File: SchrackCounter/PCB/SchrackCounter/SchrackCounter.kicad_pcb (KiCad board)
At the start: 4 copper layers, 98 x 88 mm, 61 parts, among them J1 Conn_01x02_Pin, J2 TYPE-C-31-M-12 (USB C CONN), J3 MEM2067-02-180-00-A_REVB, SW1 SW_Push, SW2 SW_Push, SW3 SW_Push, SW4 SW_Push, SW5 SW_Push, U1 LM1084-3.3, U2 LDD080AUE-101A, U3 LTD080AUE-103A, U4 LDD080AUE-101A, U5 MAX7219, U6 ESP32-S3-WROOM-2, U7 USBLC6-2SC6

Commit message: PCB update
pcb redesign
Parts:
- removed the J1 at (164.3, 128.1)
- added D2: LED, LED_SMD:LED_0805_2012Metric_Pad1.15x1.40mm_HandSolder, F.Cu at (179.8, 119.3)
- added D3: LED, LED_SMD:LED_0805_2012Metric_Pad1.15x1.40mm_HandSolder, F.Cu at (173.8, 119.3)
- added R6: 220R, Resistor_SMD:R_0805_2012Metric_Pad1.20x1.40mm_HandSolder, B.Cu at (181.7, 119.4)
- added R7: 220R, Resistor_SMD:R_0805_2012Metric_Pad1.20x1.40mm_HandSolder, B.Cu at (175.8, 119.3)
- added SW1: SW_SPST, Connector_JST:JST_XH_B2B-XH-A_1x02_P2.50mm_Vertical, F.Cu at (161.8, 126.8)
- R5: moved to B.Cu
- U5: footprint Package_DIP:DIP-24_W10.16mm -> Package_SO:SOP-24_7.5x15.4mm_P1.27mm; moved to B.Cu
- U6: moved to F.Cu
- moved BZ1 98.5 mm to (176.8, 130.6), turned to -90 degrees
- moved R5 89.4 mm to (184.2, 132.8), turned to 90 degrees
- moved U6 65.5 mm to (228.5, 103.6), turned to -90 degrees
- moved TP1 48.1 mm to (240.0, 65.6)
- moved C8 37.6 mm to (234.5, 95.8)
- moved R14 37.5 mm to (234.5, 93.8)
- moved C7 37.3 mm to (234.2, 97.9)
- moved D4 32.1 mm to (233.5, 72.1)
- moved D5 32.1 mm to (233.5, 80.1)
- moved D6 32.1 mm to (233.5, 76.1)
- moved D7 32.1 mm to (233.5, 68.1)
- moved R12 31.7 mm to (218.2, 130.3), turned to 90 degrees
- moved U2 31.3 mm to (156.7, 86.5)
- moved U4 31.3 mm to (193.3, 86.5)
- moved U3 28.0 mm to (156.6, 114.3)
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- renumbered D2 to D4, D3 to D5, D4 to D6, D5 to D7, J2 to J1, J3 to J2, R8 to R10, R9 to R11, R10 to R12, R11 to R13, R12 to R14, R13 to R15, R14 to R16, R6 to R8, R7 to R9, SW1 to SW2, SW2 to SW3, SW3 to SW4, SW4 to SW5, SW5 to SW6
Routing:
- net CLK: track 85.5 -> 1.07 mm
- net SEG_DP: track 75.6 -> 0.00 mm
- net SEG_E: track 74.2 -> 0.00 mm
- net SEG_C: track 73.0 -> 0.00 mm
- net SEG_G: track 71.4 -> 0.00 mm
- net SEG_B: track 71.2 -> 0.00 mm
- net SEG_F: track 70.2 -> 0.00 mm
- net SEG_D: track 70.1 -> 0.00 mm
- net SEG_A: track 69.5 -> 0.00 mm
- net MODE: track 61.5 -> 5.29 mm
- net MOSI: track 53.6 -> 1.09 mm
- net LED_EXT1: track 51.8 -> 0.00 mm
- net ~{CS0}: track 49.0 -> 0.00 mm
- net SCHRACK_SW: track 53.5 -> 5.12 mm
- net LED_EXT2: track 40.8 -> 0.00 mm
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
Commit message: PCB update
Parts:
- moved C5 3.92 mm to (224.1, 70.1)
- moved C6 3.92 mm to (226.2, 70.7)
- moved R1 3.92 mm to (226.2, 74.5)
- moved R10 3.86 mm to (230.2, 85.1)
- moved R11 3.86 mm to (228.2, 85.1)
- moved U5 3.86 mm to (233.2, 73.3)
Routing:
- net SEG_E: track 0.00 -> 146.6 mm, vias 0 -> 6
- net SEG_F: track 0.00 -> 143.8 mm, vias 0 -> 6
- net SEG_A: track 0.00 -> 142.6 mm, vias 0 -> 6
- net SEG_D: track 0.00 -> 141.4 mm, vias 0 -> 5
- net SEG_B: track 0.00 -> 129.9 mm, vias 0 -> 5
- net SEG_DP: track 0.00 -> 127.6 mm, vias 0 -> 5
- net SEG_G: track 0.00 -> 125.0 mm, vias 0 -> 6
- net SEG_C: track 0.00 -> 121.3 mm, vias 0 -> 5
- net DIG_4: track 0.00 -> 77.8 mm
- net +5V: track 0.00 -> 77.8 mm, vias 2 -> 3
- net DIG_5: track 0.00 -> 71.7 mm
- net DIG_0: track 0.00 -> 68.5 mm
- net DIG_1: track 0.00 -> 64.1 mm
- net DIG_6: track 0.00 -> 54.1 mm
- net DIG_2: track 0.00 -> 30.6 mm
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
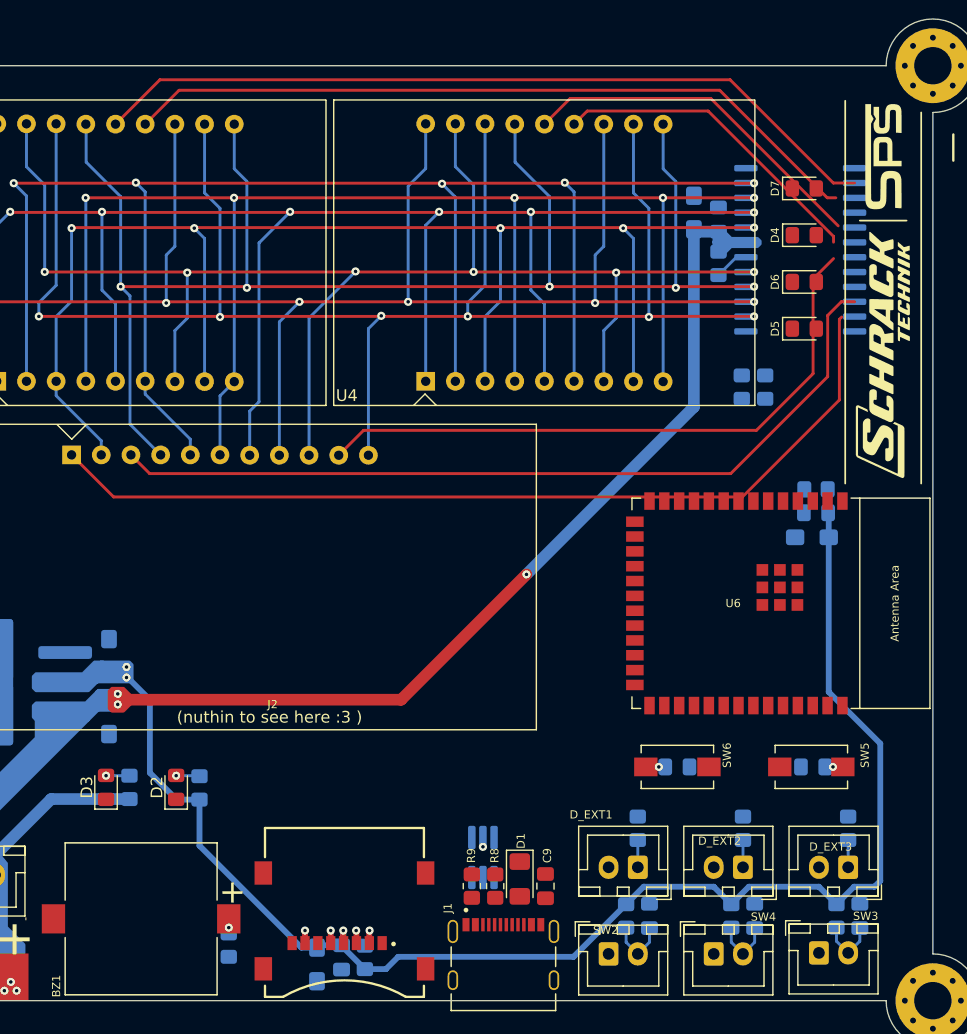
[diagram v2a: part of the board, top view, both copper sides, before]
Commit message: PCB LAYOUT UPDATE
Routing, gnd planes
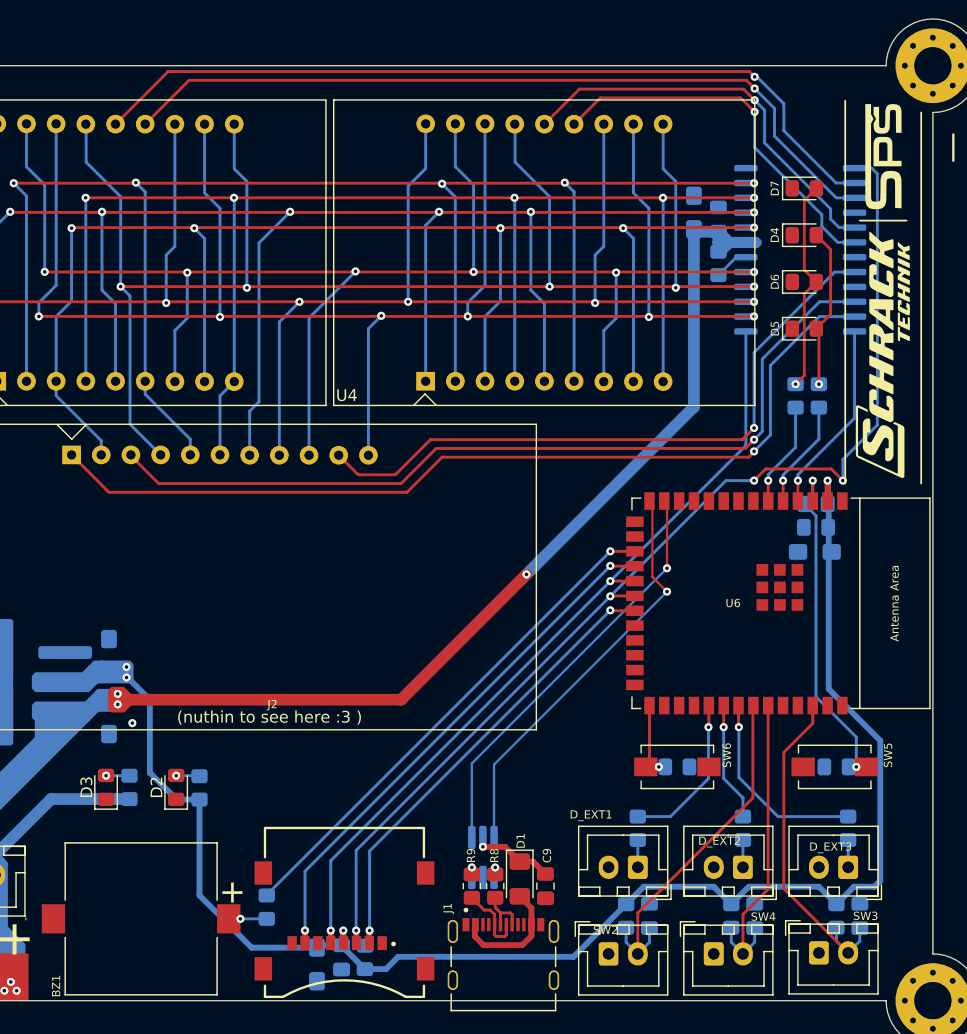
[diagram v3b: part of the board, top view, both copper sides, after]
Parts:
- moved R10 4.66 mm to (234.8, 85.8)
- moved R11 4.66 mm to (232.8, 85.8)
- moved R5 4.60 mm to (187.5, 129.6), turned to -90 degrees
- moved C12 2.00 mm to (236.2, 117.6)
- moved SW5 2.00 mm to (236.1, 117.6)
- moved C7 1.27 mm to (234.4, 99.2)
- moved C8 1.25 mm to (234.5, 97.1)
- moved R14 1.25 mm to (234.5, 95.1)
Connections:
- U5 pad 11: DIG_1 -> DIG_4
- U5 pad 3: DIG_4 -> DIG_1
- U5 pad 5: DIG_6 -> DIG_2
- U5 pad 6: DIG_2 -> DIG_3
- U5 pad 7: DIG_3 -> unconnected-(U5-DIG_3-Pad7)
- U5 pad 8: unconnected-(U5-DIG_7-Pad8) -> DIG_6
- U6 pad 12: BZ1_PWM -> unconnected-(U6-IO8-Pad12)
- U6 pad 17: GREEN_FLASH -> BZ1_PWM
- U6 pad 22: RED_FLASH -> unconnected-(U6-IO14-Pad22)
- U6 pad 23: LED_EXT3 -> unconnected-(U6-IO21-Pad23)
- U6 pad 31: LED_EXT2 -> LED_EXT1
- U6 pad 32: LED_EXT1 -> LED_EXT2
- U6 pad 33: MODE -> LED_EXT3
- U6 pad 34: SCHRACK_SW -> MODE
- U6 pad 38: unconnected-(U6-IO2-Pad38) -> SCHRACK_SW
- U6 pad 5: unconnected-(U6-IO5-Pad5) -> RED_FLASH
- U6 pad 6: unconnected-(U6-IO6-Pad6) -> GREEN_FLASH
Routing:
- net MOSI: track 1.09 -> 95.3 mm, vias 1 -> 4
- net CLK: track 1.07 -> 69.2 mm, vias 1 -> 2
- net MISO: track 1.07 -> 45.2 mm, vias 1 -> 2
- net BZ1_PWM: track 0.00 -> 43.8 mm, vias 0 -> 1
- net ~{CS1}: track 1.05 -> 39.1 mm, vias 1 -> 2
- net D-: track 0.00 -> 35.8 mm, vias 0 -> 1
- net D+: track 0.00 -> 35.5 mm, vias 0 -> 1
- net EN: track 0.00 -> 28.4 mm, vias 1 -> 2
- net MODE: track 5.29 -> 30.6 mm
- net SCHRACK_SW: track 5.12 -> 29.6 mm
- net RESET: track 5.29 -> 27.4 mm
- net Net-(D6-A): track 0.00 -> 18.3 mm, vias 0 -> 1
- net LED_EXT3: track 0.00 -> 16.9 mm, vias 0 -> 1
- net ~{CS0}: track 0.00 -> 16.5 mm, vias 0 -> 1
- net LED_EXT1: track 0.00 -> 13.9 mm, vias 0 -> 1
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
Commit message: pcb layput and routong update
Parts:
- moved D3 21.5 mm to (195.2, 118.3)
- moved D2 10.3 mm to (190.0, 118.3)
- moved R5 2.93 mm to (184.8, 128.6), turned to 180 degrees
- moved R7 2.70 mm to (177.2, 121.6), turned to -90 degrees
- moved R6 2.53 mm to (180.5, 121.6), turned to -90 degrees
- moved BZ1 2.02 mm to (176.5, 128.6), turned to 0 degrees
- moved C10 2.00 mm to (218.2, 130.3)
- moved C11 2.00 mm to (236.2, 130.3)
- moved C13 2.00 mm to (227.2, 130.3)
- moved D_EXT1 2.00 mm to (217.2, 126.1)
- moved D_EXT2 2.00 mm to (226.2, 126.1)
- moved D_EXT3 2.00 mm to (235.2, 126.1)
- moved R12 2.00 mm to (216.2, 130.3)
- moved R13 2.00 mm to (234.2, 130.3)
- moved R15 2.00 mm to (225.2, 130.3)
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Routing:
- net GND: track 0.00 -> 20.8 mm, vias 1 -> 3
- net Net-(D3-A): track 2.02 -> 21.9 mm, vias 1 -> 3
- net Net-(D2-A): track 2.04 -> 11.7 mm
- net Net-(BZ1-+): track 3.00 -> 12.2 mm
- net MODE: track 30.6 -> 34.3 mm
- net +3V3: track 130.6 -> 132.8 mm
- net ~{CS1}: track 39.1 -> 41.1 mm
- net SCHRACK_SW: track 29.6 -> 27.9 mm
- net MOSI: track 95.3 -> 96.9 mm
- net LED_EXT1: track 13.9 -> 15.5 mm
- net BZ1_PWM: track 43.8 -> 45.3 mm
- net LED_EXT3: track 16.9 -> 15.5 mm
- net +5V: track 77.8 -> 76.6 mm
- net LED_EXT2: track 10.2 -> 9.11 mm
- net RESET: track 27.4 -> 28.2 mm
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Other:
- board size 98 x 88 mm -> 98.5 x 88.5 mm

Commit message: PCB finalizing
Final routing and layout
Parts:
- moved R6 15.3 mm to (195.2, 117.6)
- moved R7 13.6 mm to (190.2, 117.6)
- moved SW6 8.48 mm to (214.2, 118.8), turned to 0 degrees
- moved C14 7.74 mm to (215.0, 118.8), turned to 180 degrees
- moved D2 7.29 mm to (197.2, 117.6)
- moved D3 7.04 mm to (188.2, 117.6)
- moved C12 1.46 mm to (235.5, 118.8), turned to 0 degrees
- moved SW5 1.25 mm to (236.2, 118.8), turned to 180 degrees
- moved TP1 0.79 mm to (240.2, 66.3)
- moved SW1 0.77 mm to (163.5, 125.8)
- moved TP2 0.56 mm to (240.5, 82.8)
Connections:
- D2 pad 1: GND -> Net-(D2-K)
- D2 pad 2: Net-(D2-A) -> +3V3
- D3 pad 1: GND -> Net-(D3-K)
- D3 pad 2: Net-(D3-A) -> VBATT
- R6 pad 1: +3V3 -> Net-(D2-K)
- R6 pad 2: Net-(D2-A) -> GND
- R7 pad 1: VBATT -> Net-(D3-K)
- R7 pad 2: Net-(D3-A) -> GND
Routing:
- net Net-(D3-A): track 21.9 -> 0.00 mm, vias 3 -> 0
- net +3V3: track 132.8 -> 145.7 mm, vias 4 -> 5
- net VBATT: track 15.3 -> 28.2 mm, vias 3 -> 6
- net Net-(D2-A): track 11.7 -> 0.00 mm, vias 1 -> 0
- net Net-(D2-K): track 0.00 -> 3.29 mm, vias 0 -> 1
- net Net-(D3-K): track 0.00 -> 2.83 mm, vias 0 -> 1
- net BOOT: track 6.49 -> 8.63 mm
- net Net-(BZ1-+): track 12.2 -> 11.5 mm
- net GND: vias 3 -> 4
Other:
- board text added: "BOOT"
- board text added: "D_EXT1"
- board text added: "D_EXT2"
- board text added: "D_EXT3"
- board text added: "EN"
- board text added: "MADE BY BISMARX"
- board text added: "PWR_SW"
- board text added: "SCH_SW"
- board text added: "SCORE"
- board text added: "TIME"
- board text added: "VCC"
- board text added: "VDD"
- board text removed: "MADE BY SAVVA POPOV"

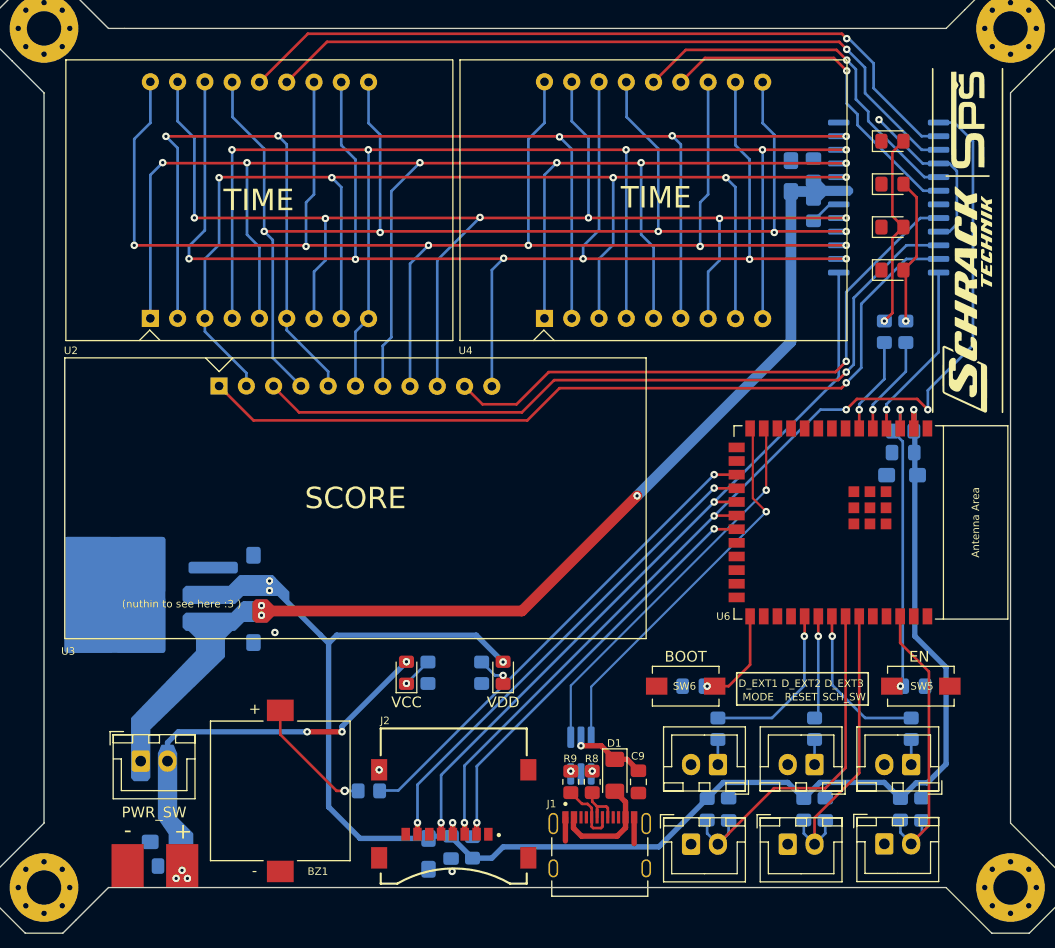
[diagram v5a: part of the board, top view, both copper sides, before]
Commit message: SchrackMulticlock and Counter update
Schematic update for both
PCB update for Counter
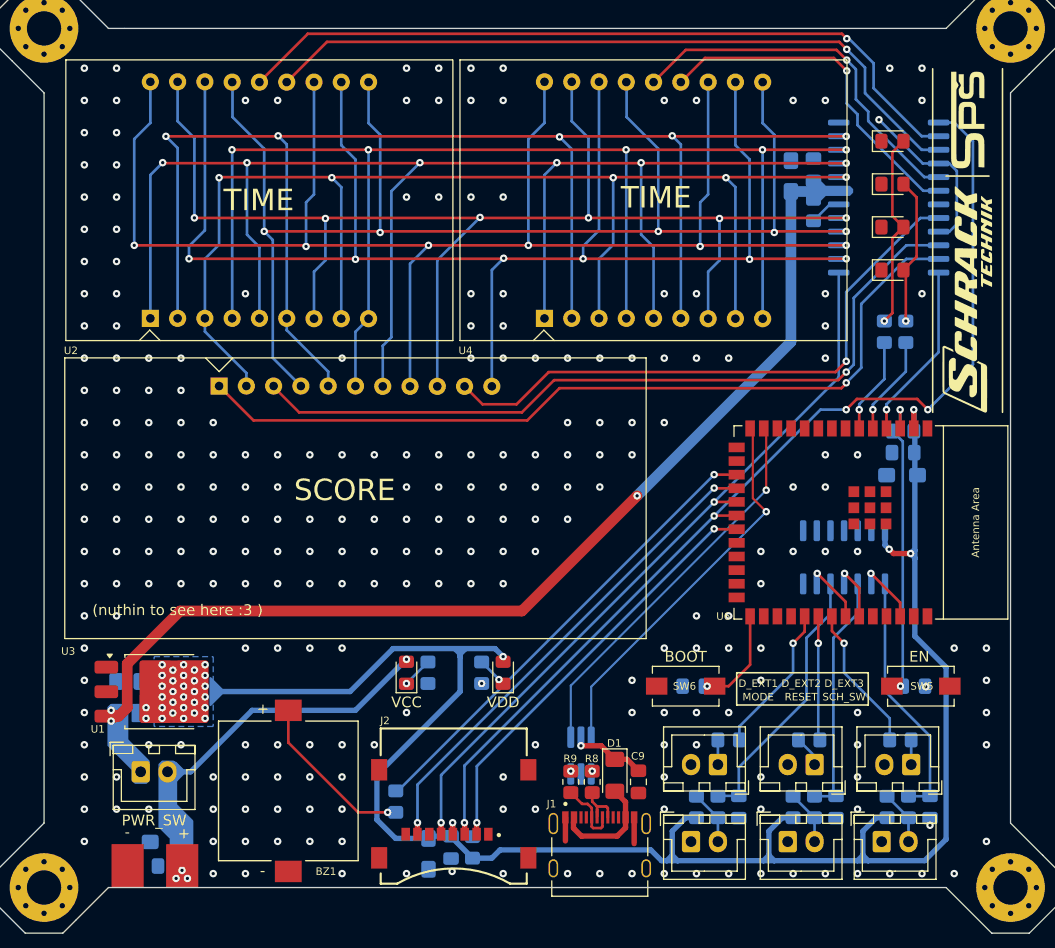
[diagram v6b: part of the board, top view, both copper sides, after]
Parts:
- added R14: 10k, Resistor_SMD:R_0805_2012Metric_Pad1.20x1.40mm_HandSolder, B.Cu at (217.2, 130.1)
- added R17: 10k, Resistor_SMD:R_0805_2012Metric_Pad1.20x1.40mm_HandSolder, B.Cu at (233.0, 130.1)
- added R18: 10k, Resistor_SMD:R_0805_2012Metric_Pad1.20x1.40mm_HandSolder, B.Cu at (235.0, 130.1)
- added U8: 74HC14, Package_SO:SOIC-14_3.9x8.7mm_P1.27mm, B.Cu at (229.0, 106.8)
- C12: value 100nF.en -> 100nF
- C14: value 100nF.boot -> 100nF
- J2: value MEM2067-02-180-00-A_REVB -> MEM2067-02-180-00
- R12, R13, R15: value 2k -> 10k
- R16: renamed from R14; value 10k.mcu -> 10k
- U1: value LM1084-3.3 -> LM1117DT-3.3; footprint Package_TO_SOT_SMD:TO-263-3_TabPin2 -> Package_TO_SOT_SMD:TO-252-3_TabPin2; moved to F.Cu
- moved C4 15.8 mm to (163.5, 119.8)
- moved C1 14.3 mm to (161.2, 119.8), turned to 90 degrees
- moved R13 10.0 mm to (224.2, 130.1), turned to -90 degrees
- moved C13 9.75 mm to (237.0, 130.1), turned to 90 degrees
- moved U1 9.42 mm to (165.3, 119.3), turned to 0 degrees
- moved SW3 9.00 mm to (223.8, 133.3)
- moved SW4 8.75 mm to (232.5, 133.3)
- moved C11 8.00 mm to (228.2, 130.1), turned to 90 degrees
- moved R5 2.69 mm to (187.2, 129.6), turned to -90 degrees
- moved R2 1.44 mm to (218.2, 123.8), turned to 0 degrees
- moved R4 1.44 mm to (234.2, 123.8), turned to 180 degrees
- moved R3 1.15 mm to (225.8, 123.8), turned to 0 degrees
- moved R12 1.02 mm to (215.2, 130.1), turned to -90 degrees
- moved R15 1.02 mm to (226.2, 130.1), turned to -90 degrees
- moved SW1 1.00 mm to (163.5, 126.8)
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- renumbered R16 to R19
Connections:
- net Net-(D_EXT1-Pin_1) renamed /CONNECTIVITY/EXT1
- net Net-(D_EXT2-Pin_1) renamed /CONNECTIVITY/EXT2
- net Net-(D_EXT3-Pin_1) renamed /CONNECTIVITY/EXT3
- C10 pad 2: MODE -> Net-(C10-Pad2)
- C11 pad 2: SCHRACK_SW -> Net-(C11-Pad2)
- C13 pad 2: RESET -> Net-(C13-Pad2)
- R12 pad 1: MODE -> /MECHANICS/MD
- R13 pad 1: SCHRACK_SW -> /MECHANICS/RST
- R15 pad 1: RESET -> Net-(C11-Pad2)
- R15 pad 2: +3V3 -> /MECHANICS/RST
- SW2 pad 2: MODE -> /MECHANICS/MD
- SW3 pad 2: SCHRACK_SW -> /MECHANICS/RST
- SW4 pad 2: RESET -> /MECHANICS/SCH_SW
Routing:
- net +3V3: track 145.7 -> 177.9 mm, vias 5 -> 35
- net MODE: track 34.3 -> 5.15 mm, vias 0 -> 1
- net Net-(C10-Pad2): track 0.00 -> 25.2 mm
- net RESET: track 28.2 -> 4.58 mm, vias 0 -> 1
- net Net-(C13-Pad2): track 0.00 -> 23.5 mm
- net SCHRACK_SW: track 28.0 -> 5.13 mm, vias 0 -> 1
- net Net-(C11-Pad2): track 0.00 -> 22.8 mm
- net +5V: track 76.6 -> 98.5 mm
- net /MECHANICS/RST: track 0.00 -> 5.26 mm
- net /MECHANICS/SCH_SW: track 0.00 -> 5.05 mm
- net /MECHANICS/MD: track 0.00 -> 5.05 mm
- net Net-(BZ1-+): track 11.5 -> 15.7 mm
- net LED_EXT2: track 8.96 -> 11.6 mm
- net LED_EXT3: track 15.5 -> 13.7 mm
- net BZ1_PWM: track 45.3 -> 43.7 mm
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- added copper zone on B.Cu, net +3V3

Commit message: SchrackMulticlock update
Schematic and PCB update
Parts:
- added C9: 100nF, Capacitor_SMD:C_0805_2012Metric_Pad1.18x1.45mm_HandSolder, B.Cu at (204.6, 129.9)
- added R5: 100k, Resistor_SMD:R_0805_2012Metric_Pad1.20x1.40mm_HandSolder, B.Cu at (204.6, 131.9)
- renumbered C9 to C10, C10 to C11, C11 to C12, C12 to C13, C13 to C14, C14 to C15, C15 to C16, C16 to C17, R9 to R10, R10 to R11, R11 to R12, R12 to R13, R13 to R14, R14 to R15, R15 to R16, R16 to R17, R17 to R18, R18 to R19, R19 to R20, R5 to R6, R6 to R7, R7 to R8, R8 to R9
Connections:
- J1 pad S1: unconnected-(J1-SHIELD-PadS1)_3 -> /CONNECTIVITY/SHLD
- J1 pad S2: unconnected-(J1-SHIELD-PadS1)_1 -> /CONNECTIVITY/SHLD
- J1 pad S3: unconnected-(J1-SHIELD-PadS1)_2 -> /CONNECTIVITY/SHLD
- J1 pad S4: unconnected-(J1-SHIELD-PadS1) -> /CONNECTIVITY/SHLD
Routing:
- net /CONNECTIVITY/SHLD: track 0.00 -> 21.7 mm
- net GND: vias 257 -> 254
